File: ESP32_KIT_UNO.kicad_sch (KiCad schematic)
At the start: 55 parts, among them J1 Conn_01x06_Pin, J3 Conn_01x06_Pin, J4 Jack DC, J5 Conn_01x06_Pin, Q1 BC817, Q2 BC817, U1 ESP32-WROOM-32, U2 CH340C, U3 AMS1117-3.3, U5 MP1482DS-LF-Z, U6 LMV321

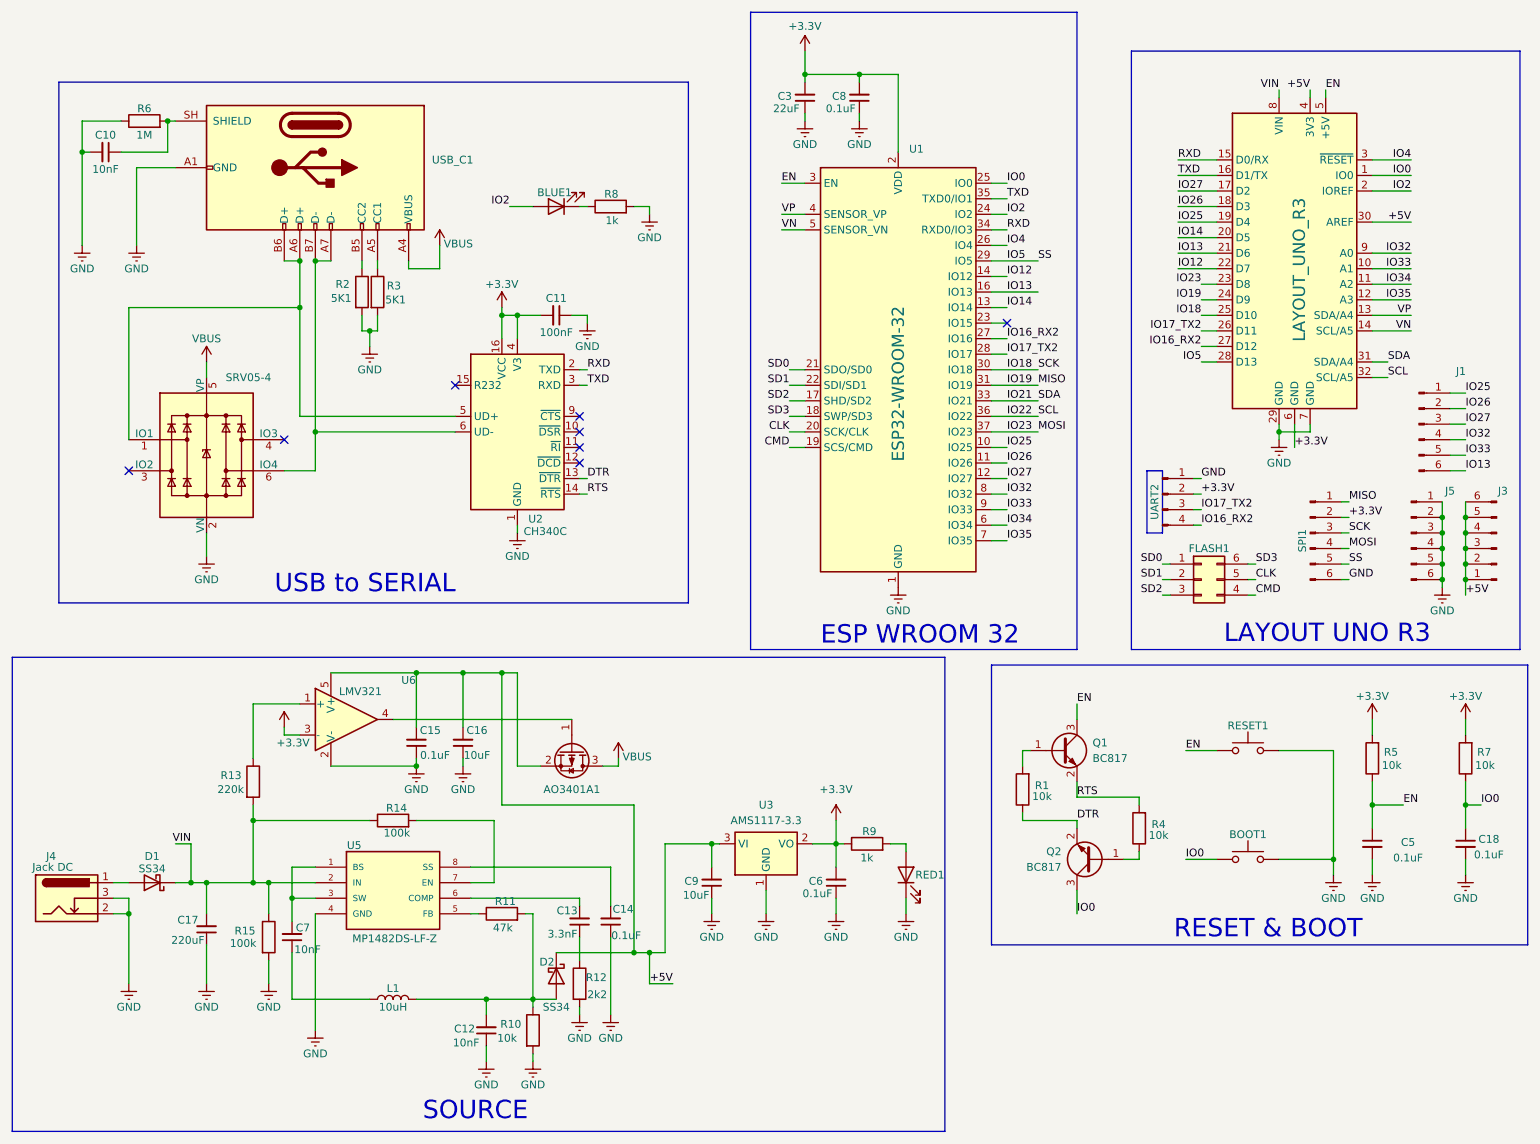
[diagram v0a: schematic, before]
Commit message: Cap nhat file thiet ke KiCad va xuat file Gerber PDF
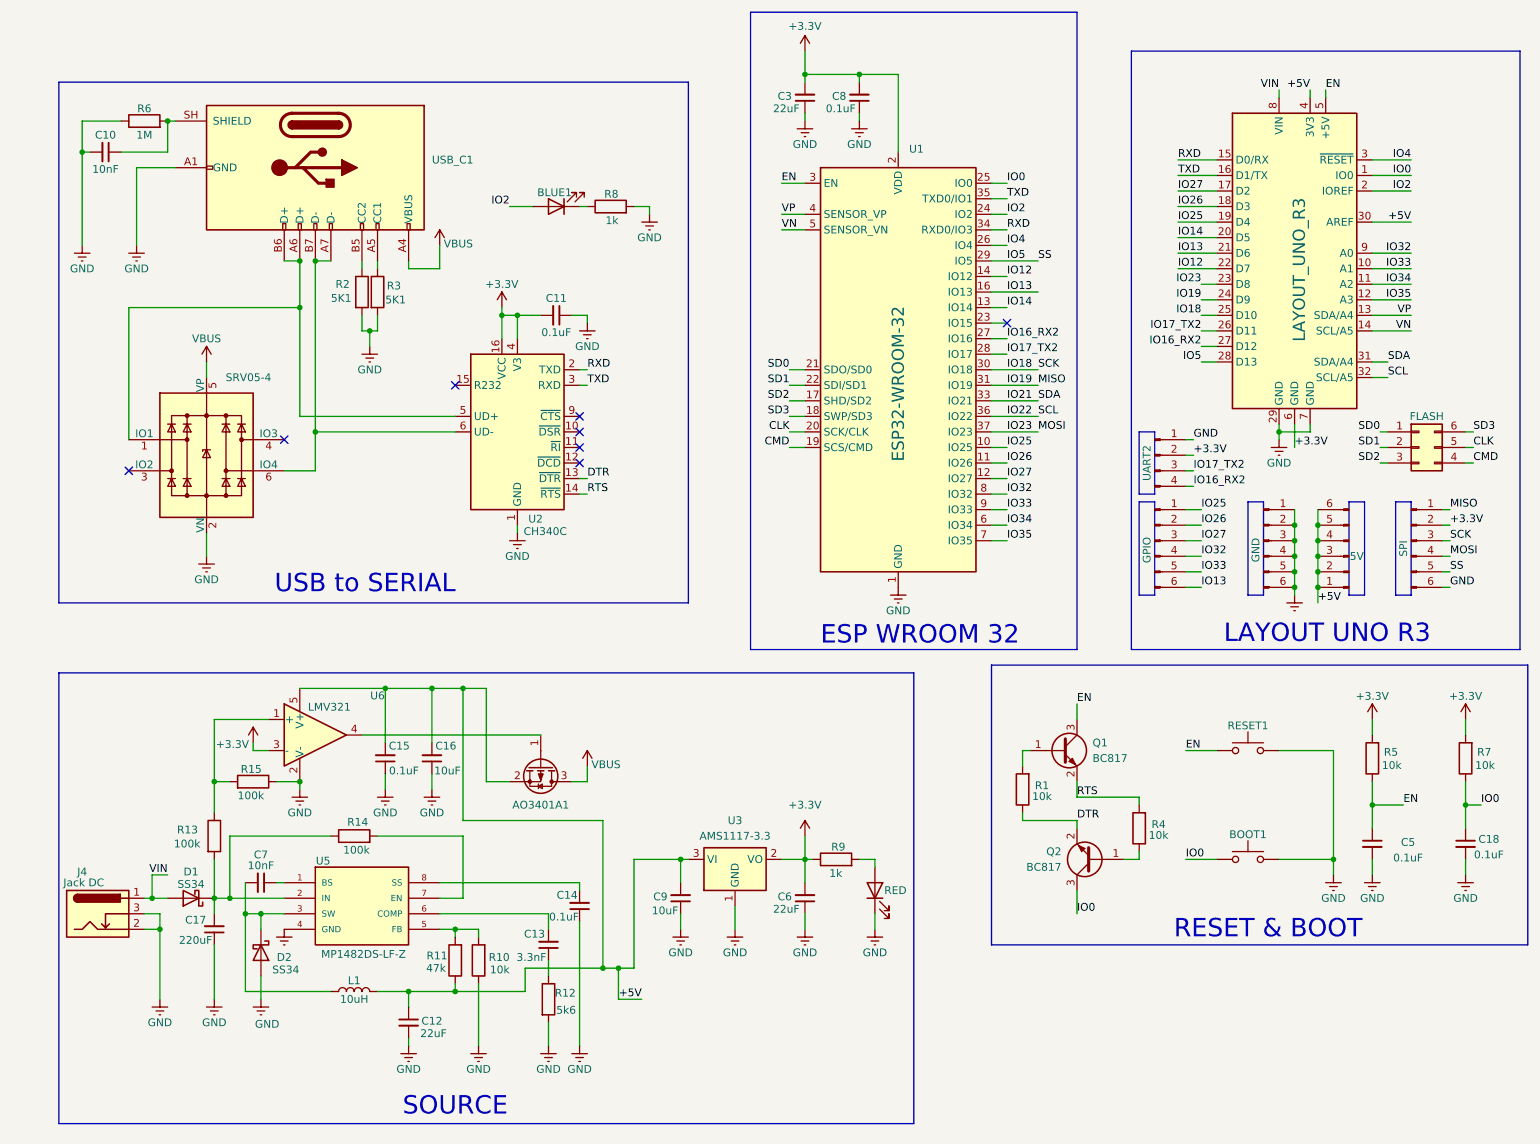
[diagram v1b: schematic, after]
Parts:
- C11: value 100nF -> 0.1uF
- C12: value 10nF -> 22uF
- C6: value 0.1uF -> 22uF
- R12: value 2k2 -> 5k6
- R13: value 220k -> 100k
- renumbered J3 to 5V, FLASH1 to FLASH, J5 to GND, J1 to GPIO, RED1 to RED, SPI1 to SPI
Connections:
- net +5V: now also C12.1, L1.2, R11.1; no longer D2.1 (K)
- net GND: now also C12.2, D2.2 (A), R10.1, R15.1; no longer C12.1, R10.2, R15.2
- net VIN: now also D1.2 (A), J4.1; no longer C17.2, D1.1 (K), R13.2, R14.1, R15.1, U5.2 (IN)
- net at C7.1: now also U5.1 (BS); no longer L1.1
- net at C7.2, U5.3 (SW): now also D2.1 (K), L1.1; no longer U5.1 (BS)
- net at R13.1, U6.1 (+): now also R15.2
- net at U5.5 (FB): now also R10.2, R11.2; no longer R11.1
- new net: C17.2, D1.1 (K), R13.2, R14.1, U5.2 (IN)
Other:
- moved on the sheet: 5V, AO3401A1, C12, C13, C14, C15, C16, C17, C6, C9, D1, FLASH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
